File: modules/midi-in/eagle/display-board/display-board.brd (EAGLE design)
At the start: 79.7 x 55.9 mm, 21 parts

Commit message: Added shift registers, start-up reset on display board schematic
TODO: revise the board, revise the main schematic
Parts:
- removed JP1: (no value), pinhead:1X01
- removed SV2: (no value), con-lstb:MA08-1
- added C1: 100n, rcl:C050-024X044
- added R17, R18: 10k, resistor:0207/7
- added T1: BC547, transistor:TO92
- added V1, V2: 74595N, 74ttl-din:DIL16
- SV1: device con-lstb:MA08-1 -> con-lstb:MA05-1
- moved SV1 100.2 mm to (7.62, -95.2)
- moved R16 90.9 mm to (5.08, -67.3), turned to 0 degrees
- moved R10 90.8 mm to (5.08, -52.1), turned to 0 degrees
- moved R14 90.0 mm to (5.08, -62.2), turned to 0 degrees
- moved R12 89.9 mm to (5.08, -57.1), turned to 0 degrees
- moved D2 86.3 mm to (7.62, -36.8)
- moved R15 83.7 mm to (15.2, -62.2), turned to 0 degrees
- moved R13 82.4 mm to (15.2, -57.1), turned to 0 degrees
- moved R11 82.1 mm to (15.2, -52.1), turned to 0 degrees
- moved R9 66.6 mm to (20.3, -29.2), turned to 0 degrees
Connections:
- new net GND: R18.1, SV1.1, T1.1, V1.13, V1.8, V2.13, V2.8
- new net N$33: V1.9, V2.14
- new net N$34: C1.2, R18.2, V1.10, V2.10
- new net N$35: SV1.3, V1.12, V2.12
- new net N$36: SV1.4, V1.11, V2.11
- new net N$37: R17.2, T1.2
- new net N$38: SV1.5, V1.14
- new net VCC1: D2.8
- net N$10: now also R10.1; no longer R10.2
- net N$11: now also R11.1; no longer R11.2
- net N$12: now also R12.1; no longer R12.2
- net N$13: now also R13.1; no longer R13.2
- net N$14: now also R14.1; no longer R14.2
- net N$15: now also R15.1; no longer R15.2
- net N$16: now also R16.1; no longer R16.2
- net N$17: now also V1.15; no longer SV1.1
- net N$18: now also V1.1; no longer SV1.2
- net N$19: now also V1.2; no longer SV1.3
- net N$20: now also V1.3; no longer SV1.4
- net N$21: now also V1.4; no longer SV1.5
- net N$22: now also V1.5; no longer SV1.6
- net N$23: now also V1.6; no longer SV1.7
- net N$24: now also V1.7; no longer SV1.8
- net N$25: now also R9.2, V2.15; no longer R9.1, SV2.1
- net N$26: now also R10.2, V2.1; no longer R10.1, SV2.2
- net N$27: now also R11.2, V2.2; no longer R11.1, SV2.3
- net N$28: now also R12.2, V2.3; no longer R12.1, SV2.4
- net N$29: now also R13.2, V2.4; no longer R13.1, SV2.5
- net N$30: now also R14.2, V2.5; no longer R14.1, SV2.6
- net N$31: now also R15.2, V2.6; no longer R15.1, SV2.7
- net N$32: now also R16.2, V2.7; no longer R16.1, SV2.8
- net N$9: now also R9.1; no longer R9.2
- net VCC: now also C1.1, R17.1, SV1.2, T1.3, V1.16, V2.16; no longer D2.8, JP1.1
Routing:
- net N$15: track 151.1 -> 0.00 mm
- net VCC: track 118.1 -> 3.81 mm, vias 2 -> 1
- net N$10: track 53.9 -> 0.00 mm
- net N$16: track 48.0 -> 0.00 mm
- net N$9: track 45.6 -> 0.00 mm
- net N$14: track 40.9 -> 0.00 mm
- net N$12: track 27.5 -> 0.00 mm
- net N$13: track 25.0 -> 0.00 mm
- net N$11: track 25.0 -> 0.00 mm
- net N$25: track 10.3 -> 0.00 mm
- net N$26: track 9.72 -> 0.00 mm
- net N$27: track 9.20 -> 0.00 mm
- net N$17: track 10.3 -> 1.27 mm
- net N$32: track 8.67 -> 0.00 mm
- net N$28: track 8.67 -> 0.00 mm
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
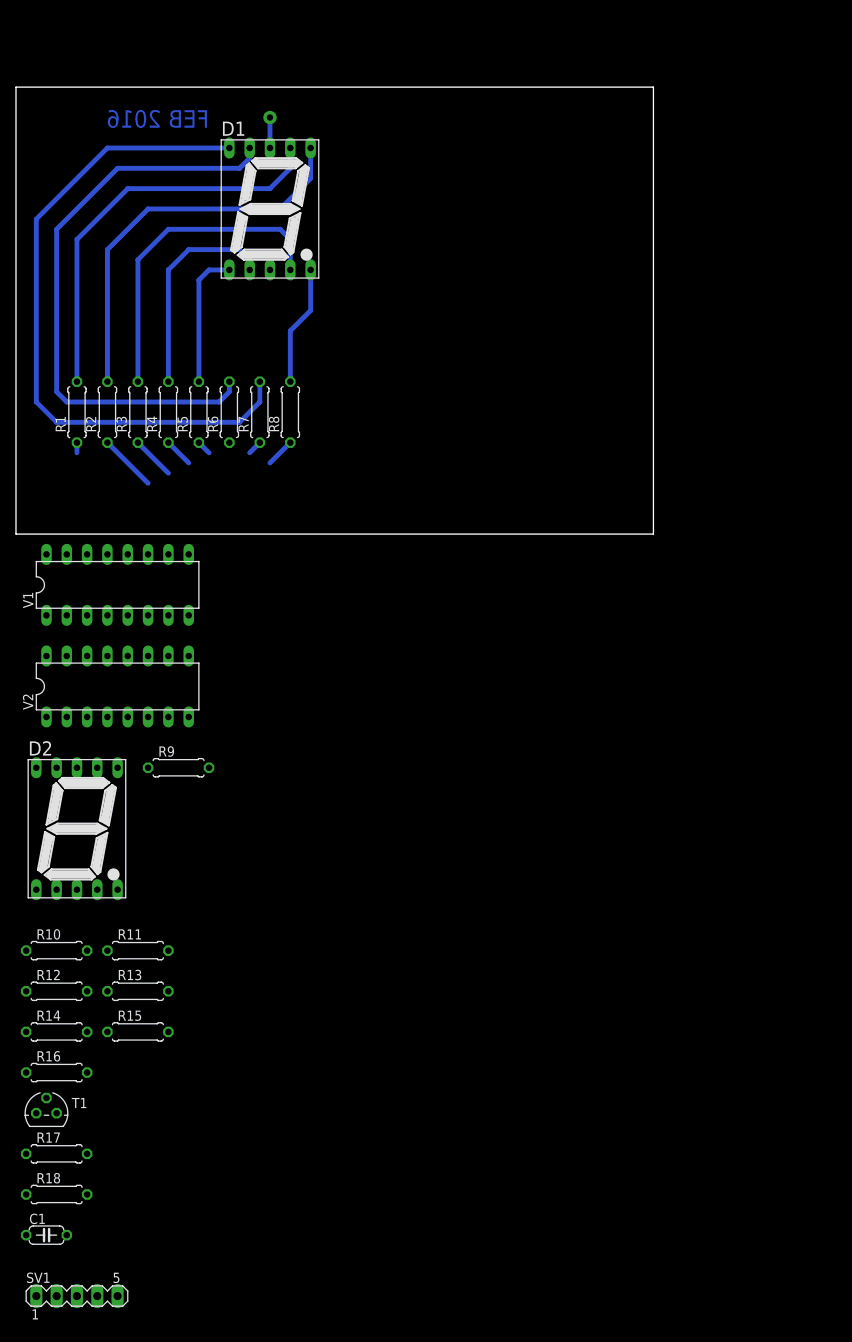
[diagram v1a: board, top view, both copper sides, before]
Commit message: Redesign display board layout w/ shift registers
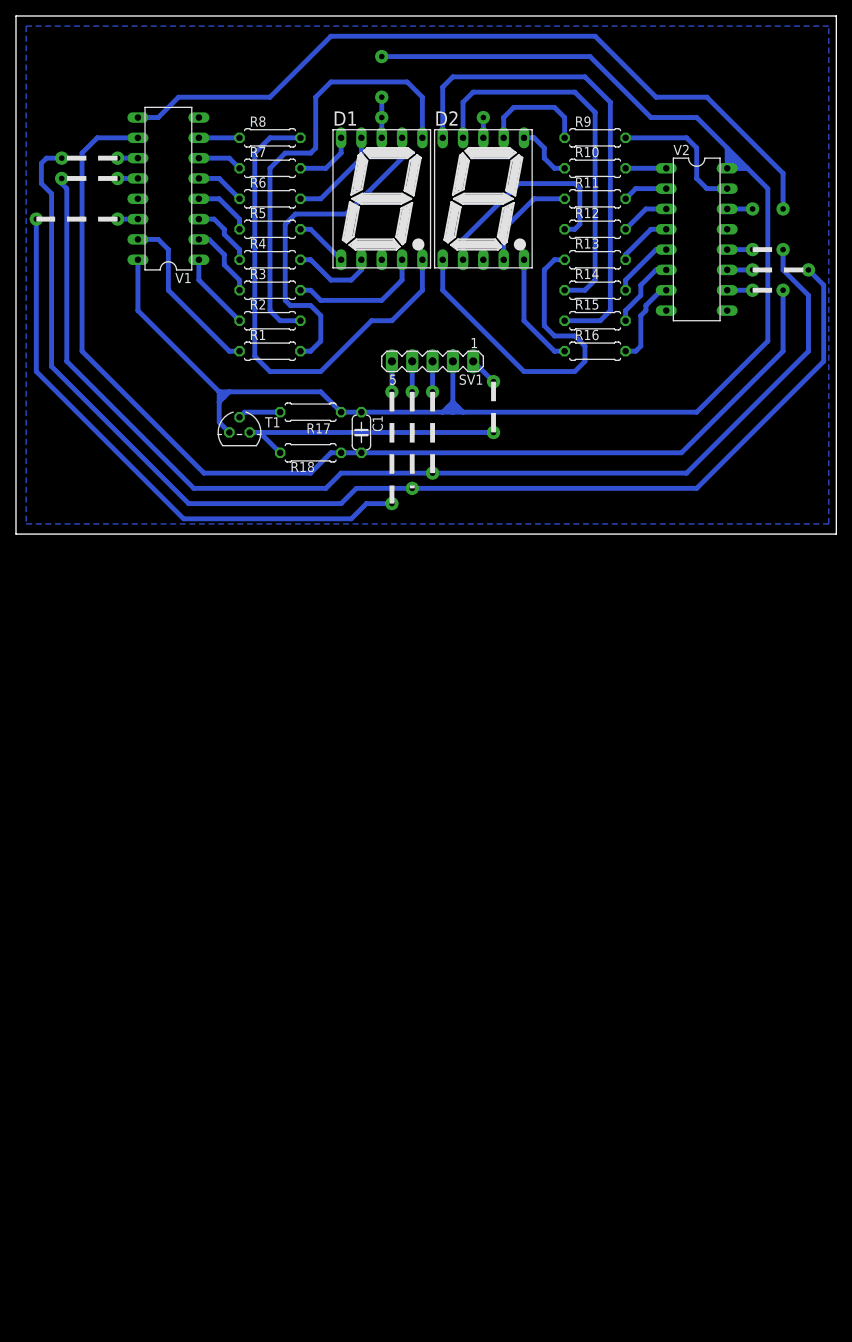
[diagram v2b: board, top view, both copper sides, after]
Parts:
- moved SV1 125.0 mm to (52.1, 21.6), turned to 180 degrees
- moved R10 118.7 mm to (72.4, 45.7)
- moved R12 116.6 mm to (72.4, 38.1)
- moved R14 114.6 mm to (72.4, 30.5)
- moved R16 112.5 mm to (72.4, 22.9)
- moved R11 110.0 mm to (72.4, 41.9)
- moved R13 107.8 mm to (72.4, 34.3)
- moved C1 107.8 mm to (43.2, 12.7), turned to 270 degrees
- moved R15 105.7 mm to (72.4, 26.7)
- moved R17 98.0 mm to (36.8, 15.2), turned to 180 degrees
- moved R18 98.0 mm to (36.8, 10.2)
- moved R9 94.4 mm to (72.4, 49.5)
- moved D2 93.7 mm to (58.4, 41.9)
- moved V2 91.4 mm to (85.1, 36.8), turned to 270 degrees
- moved T1 88.4 mm to (27.9, 12.7)
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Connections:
- net GND renamed N$46
- removed net VCC1: D2.8
- net VCC: now also D2.8
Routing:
- net VCC: track 3.81 -> 210.5 mm, vias 1 -> 0
- net N$55: track 0.00 -> 151.9 mm, vias 0 -> 3
- net N$34: track 0.00 -> 143.6 mm
- net N$49: track 0.00 -> 143.5 mm, vias 0 -> 3
- net N$33: track 0.00 -> 99.6 mm, vias 0 -> 1
- net N$7: track 83.3 -> 7.77 mm
- net N$62: track 0.00 -> 71.9 mm, vias 0 -> 2
- net N$15: track 0.00 -> 61.4 mm
- net N$6: track 73.3 -> 12.3 mm
- net N$14: track 0.00 -> 47.8 mm
- net N$8: track 15.0 -> 61.7 mm
- net N$13: track 0.00 -> 44.4 mm
- net N$46: track 0.00 -> 38.9 mm, vias 0 -> 2
- net N$12: track 0.00 -> 26.9 mm
- net N$3: track 40.2 -> 16.8 mm
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- added copper zone on layer 16, net N$46
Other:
- board size 79.7 x 55.9 mm -> 102.5 x 64.8 mm
- board text removed: "FEB 2016"
- board text removed: "VCC"

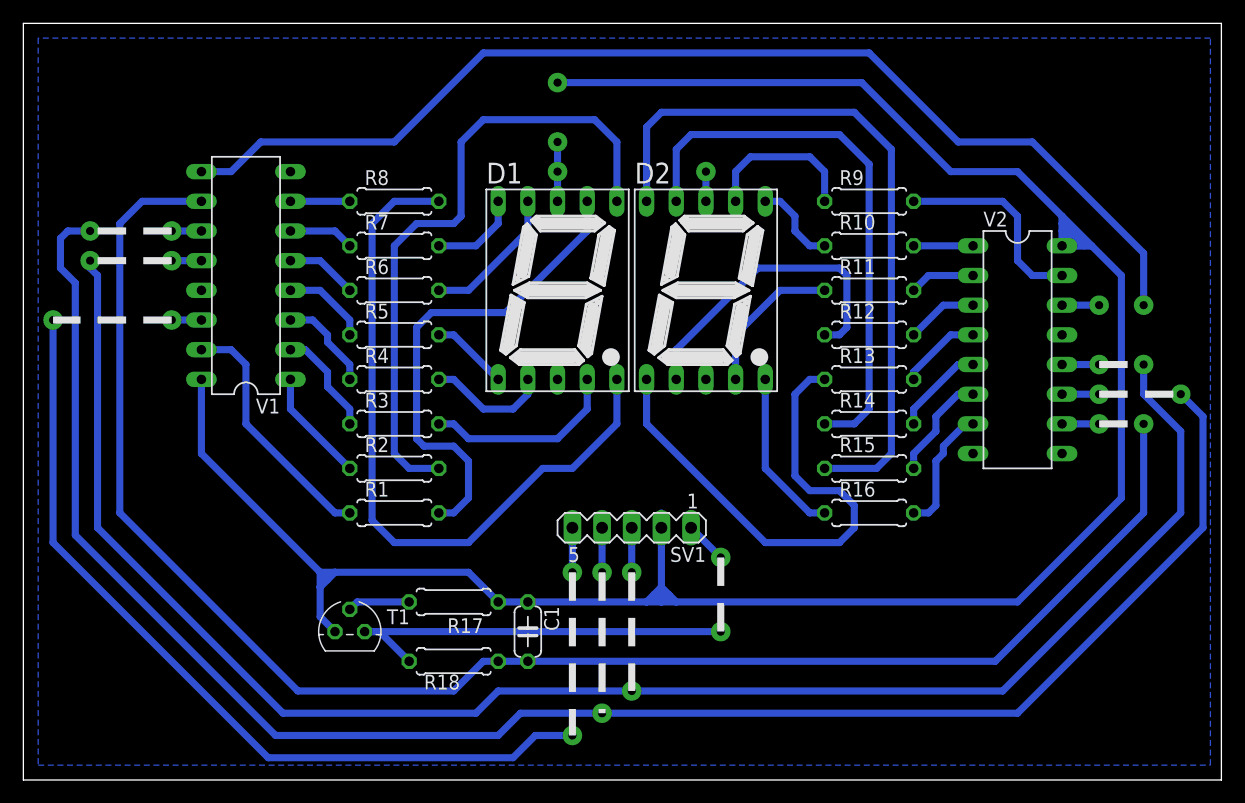
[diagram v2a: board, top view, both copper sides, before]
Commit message: Finish MIDI in display board and schematic, add readme
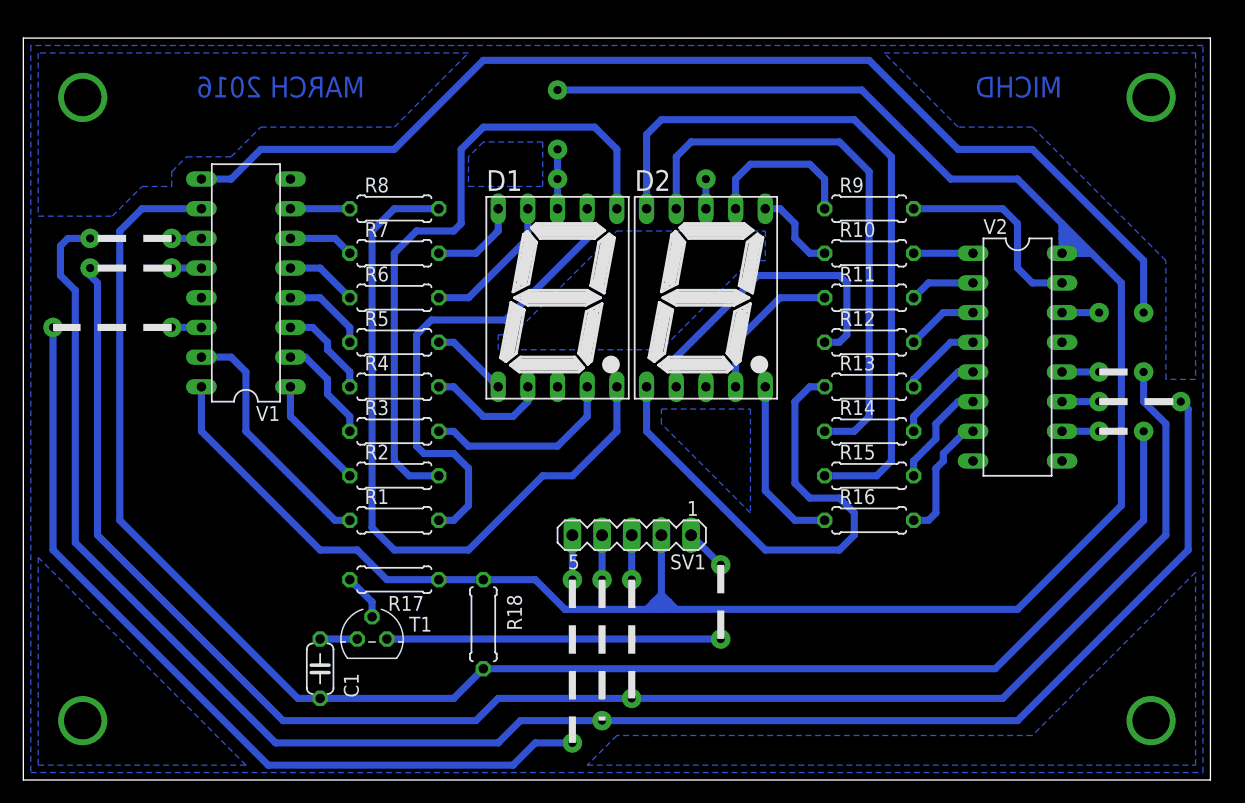
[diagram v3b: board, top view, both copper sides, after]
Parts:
- moved C1 18.1 mm to (25.4, 9.53)
- moved R17 5.43 mm to (31.8, 17.1)
- moved R18 4.07 mm to (39.4, 13.3), turned to 270 degrees
- moved T1 2.01 mm to (29.8, 12.1)
- moved R14 0.64 mm to (72.4, 29.8)
- moved R15 0.64 mm to (72.4, 26.0)
- moved R2 0.64 mm to (31.8, 26.0)
- moved R3 0.64 mm to (31.8, 29.8)
- moved SV1 0.64 mm to (52.1, 21.0)
- moved D1 0.63 mm to (45.7, 41.3)
- moved D2 0.63 mm to (58.4, 41.3)
- moved R1 0.63 mm to (31.8, 22.2)
- moved R10 0.63 mm to (72.4, 45.1)
- moved R11 0.63 mm to (72.4, 41.3)
- moved R12 0.63 mm to (72.4, 37.5)
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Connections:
- new net N$61: C1.1, T1.3
- net N$46: no longer R18.1
- net VCC: now also R18.1; no longer C1.1, T1.3
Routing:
- net VCC: track 210.5 -> 200.7 mm
- net N$46: track 38.9 -> 32.2 mm
- net N$61: track 0.00 -> 3.18 mm
- net N$37: track 5.34 -> 3.96 mm
- net N$55: track 151.9 -> 150.9 mm
- net N$49: track 143.5 -> 142.5 mm
- net N$16: track 14.3 -> 15.0 mm
- added copper zone on layer 16, net N$63
- added copper zone on layer 16, net N$64
- added copper zone on layer 16, net N$65
- added copper zone on layer 16, net N$66
- added copper zone on layer 16, net N$67
- added copper zone on layer 16, net N$68
- added copper zone on layer 16, net N$69
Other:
- board size 102.5 x 64.8 mm -> 101.6 x 63.5 mm
- board text added: "MARCH 2016"
- board text added: "MICHD"

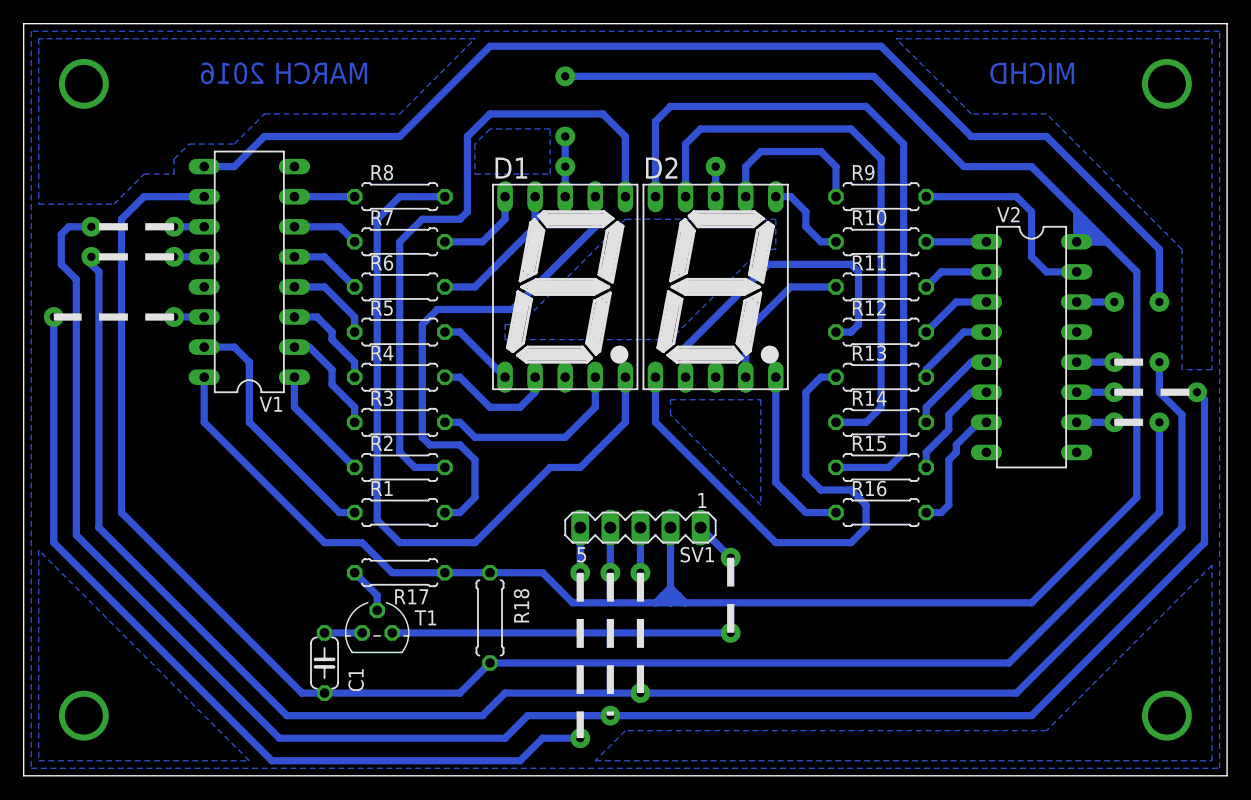
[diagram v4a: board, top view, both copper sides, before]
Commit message: Resize boards to be 10cm wide exactly
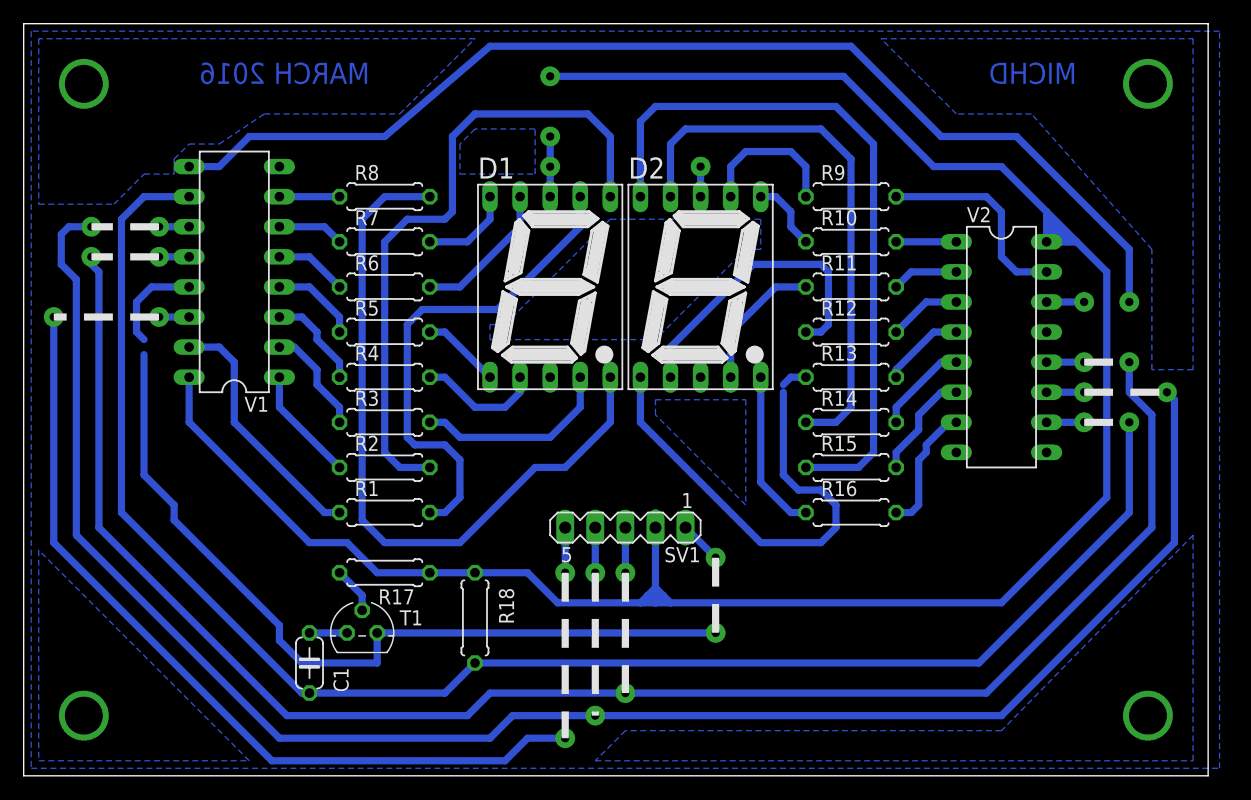
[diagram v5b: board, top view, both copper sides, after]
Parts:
- moved R10 2.54 mm to (69.8, 45.1)
- moved R11 2.54 mm to (69.8, 41.3)
- moved R12 2.54 mm to (69.8, 37.5)
- moved R13 2.54 mm to (69.8, 33.7)
- moved R14 2.54 mm to (69.8, 29.8)
- moved R15 2.54 mm to (69.8, 26.0)
- moved R16 2.54 mm to (69.8, 22.2)
- moved R9 2.54 mm to (69.8, 48.9)
- moved V2 2.54 mm to (82.5, 36.2)
- moved D2 1.27 mm to (57.1, 41.3)
- moved SV1 1.27 mm to (50.8, 21.0)
- moved C1 1.27 mm to (24.1, 9.53)
- moved R1 1.27 mm to (30.5, 22.2)
- moved R17 1.27 mm to (30.5, 17.1)
- moved R2 1.27 mm to (30.5, 26.0)
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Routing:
- net N$46: track 32.2 -> 81.0 mm
- net N$34: track 143.6 -> 139.8 mm
- net N$13: track 44.4 -> 41.6 mm
- net N$49: track 142.5 -> 139.9 mm
- net N$55: track 150.9 -> 148.3 mm
- net VCC: track 200.7 -> 198.2 mm
- net N$33: track 99.6 -> 98.0 mm
- net N$15: track 61.4 -> 60.2 mm
- net N$14: track 47.8 -> 46.6 mm
- net N$12: track 26.9 -> 25.6 mm
- net N$62: track 71.9 -> 70.6 mm
- net N$9: track 13.8 -> 12.5 mm
- net N$11: track 13.0 -> 11.7 mm
- net N$10: track 7.40 -> 6.13 mm
- net N$16: track 15.0 -> 13.8 mm
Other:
- board size 101.6 x 63.5 mm -> 100 x 63.5 mm
